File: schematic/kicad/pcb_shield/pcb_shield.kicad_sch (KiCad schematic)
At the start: 1 part, among them U1 NUCLEO64-F411RE

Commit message: pcb schematic
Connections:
- net BL_MOTOR_A: now also U1.44 (PC5); no longer U1.62 (PB1)
- net BL_MOTOR_B: now also U1.1 (PC10); no longer U1.60 (PB2)
- net BR_MOTOR_A: now also U1.2 (PC11); no longer U1.54 (PB12)
- net BR_MOTOR_B: now also U1.3 (PC12); no longer U1.44 (PC5)
- net FL_MOTOR_A: now also U1.38 (PC0); no longer U1.72 (PC4)
- net FL_MOTOR_B: now also U1.36 (PC1); no longer U1.68 (PB13)
- net FR_ENCODER_A: now also U1.51 (PA6); no longer U1.65 (PB4)
- net FR_ENCODER_B: now also U1.53 (PA7); no longer U1.57 (PC7)
- net FR_MOTOR_A: now also U1.35 (PC2); no longer U1.66 (PB14)
- net FR_MOTOR_B: now also U1.37 (PC3); no longer U1.64 (PB15)
- net GND: now also U1.19 (GND), U1.20 (GND), U1.22 (GND), U1.47 (GND), U1.58 (GND), U1.77 (GND), U1.78 (GND), U1.79 (GND), U1.80 (GND)
- net +12V: no longer names the net of U1.24 (VIN)
- net +5V: no longer names the net of U1.18 (+5V)
- net STM32_RX6: no longer names the net of U1.50 (PA12)
- net STM32_TX6 renamed TX6
- new net RX6: U1.57 (PC7)

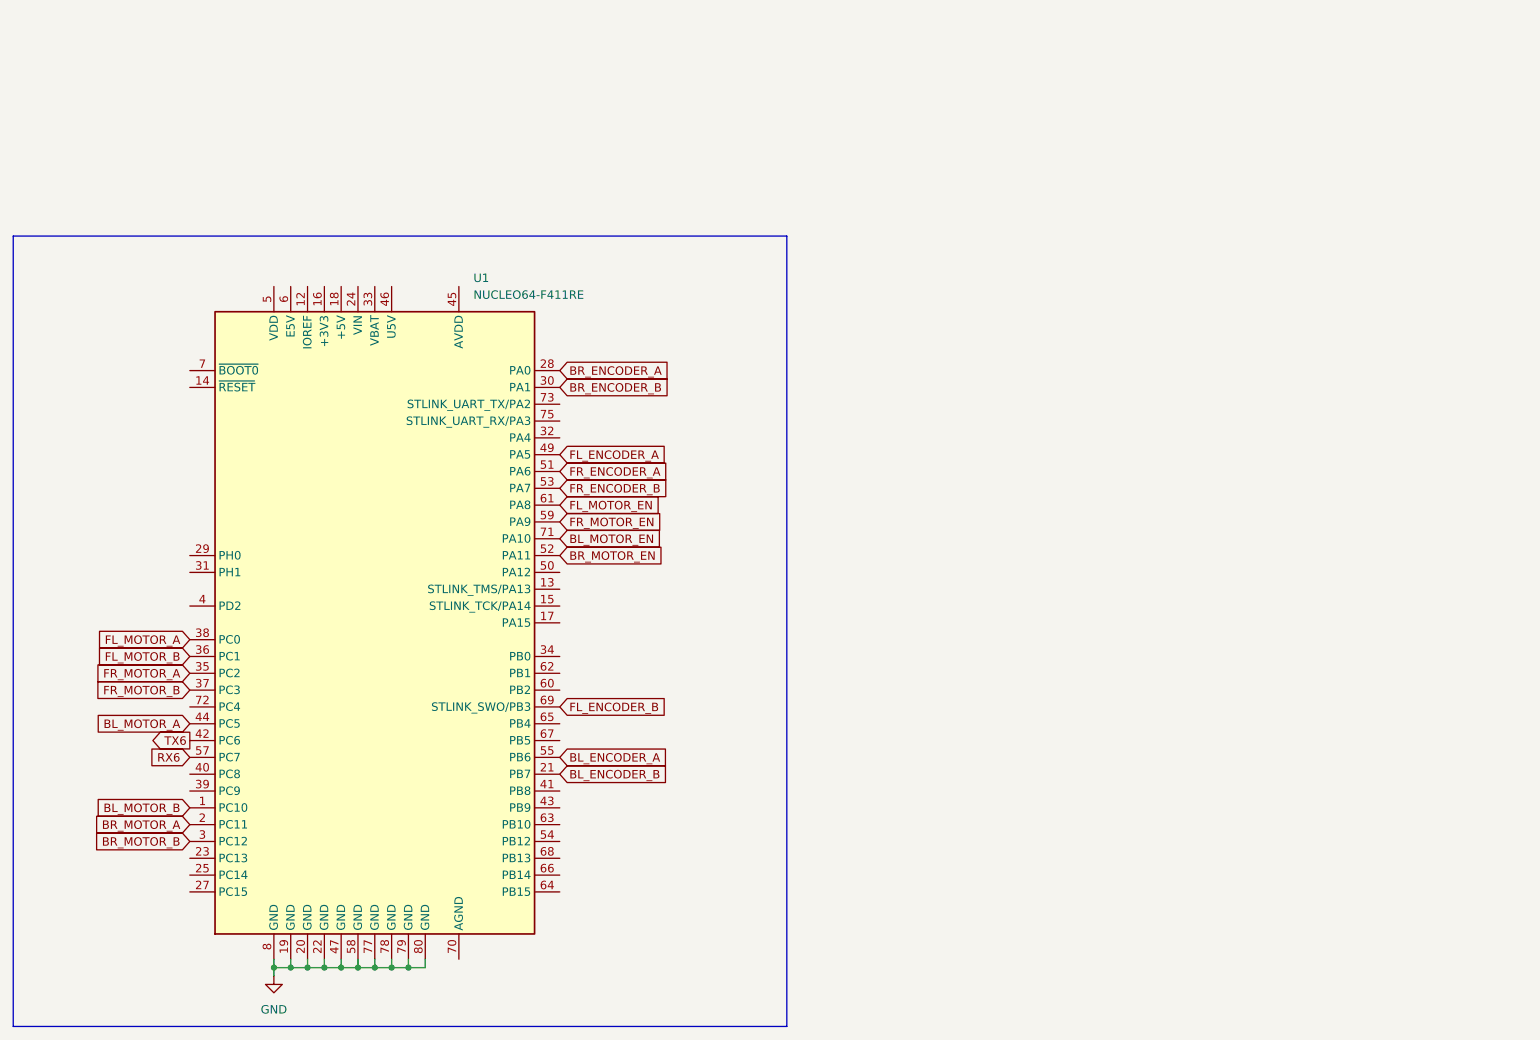
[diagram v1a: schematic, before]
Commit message: progress with code and pcb shield
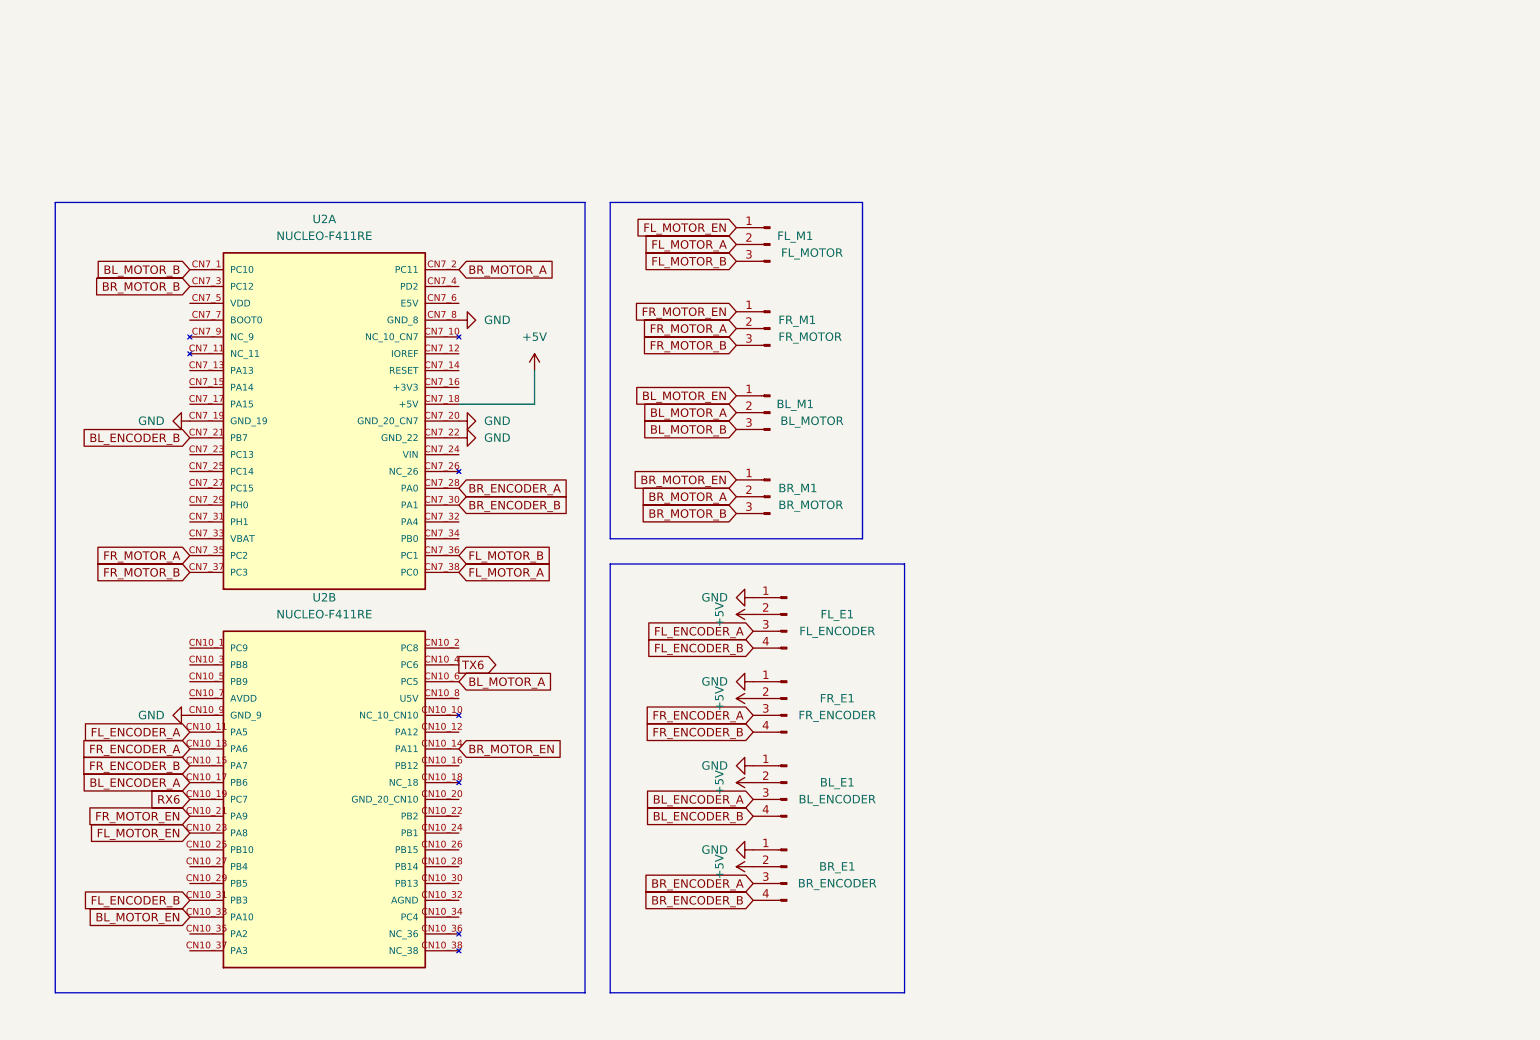
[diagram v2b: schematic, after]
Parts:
- removed U1: NUCLEO64-F411RE, Module:ST_Morpho_Connector_144_STLink, symbol MCU_Module:NUCLEO64-F411RE
- added BL_E1: BL_ENCODER, Connector_PinHeader_2.54mm:PinHeader_1x04_P2.54mm_Vertical, symbol Connector:Conn_01x04_Pin
- added BL_M1: BL_MOTOR, Connector_PinHeader_2.54mm:PinHeader_1x03_P2.54mm_Vertical, symbol Connector:Conn_01x03_Pin
- added BR_E1: BR_ENCODER, Connector_PinHeader_2.54mm:PinHeader_1x04_P2.54mm_Vertical, symbol Connector:Conn_01x04_Pin
- added BR_M1: BR_MOTOR, Connector_PinHeader_2.54mm:PinHeader_1x03_P2.54mm_Vertical, symbol Connector:Conn_01x03_Pin
- added FL_E1: FL_ENCODER, Connector_PinHeader_2.54mm:PinHeader_1x04_P2.54mm_Vertical, symbol Connector:Conn_01x04_Pin
- added FL_M1: FL_MOTOR, Connector_PinHeader_2.54mm:PinHeader_1x03_P2.54mm_Vertical, symbol Connector:Conn_01x03_Pin
- added FR_E1: FR_ENCODER, Connector_PinHeader_2.54mm:PinHeader_1x04_P2.54mm_Vertical, symbol Connector:Conn_01x04_Pin
- added FR_M1: FR_MOTOR, Connector_PinHeader_2.54mm:PinHeader_1x03_P2.54mm_Vertical, symbol Connector:Conn_01x03_Pin
- added U2: NUCLEO-F411RE, NUCLEO-F411RE:BOARD_NUCLEO-F411RE_custom, symbol NUCLEO-F411RE:NUCLEO-F411RE
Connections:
- net BL_ENCODER_A: now also BL_E1.3 (Pin_3), U2.CN10_17 (PB6)
- net BL_ENCODER_B: now also BL_E1.4 (Pin_4), U2.CN7_21 (PB7)
- net BL_MOTOR_A: now also BL_M1.2 (Pin_2), U2.CN10_6 (PC5)
- net BL_MOTOR_B: now also BL_M1.3 (Pin_3), U2.CN7_1 (PC10)
- net BL_MOTOR_EN: now also BL_M1.1 (Pin_1), U2.CN10_33 (PA10)
- net BR_ENCODER_A: now also BR_E1.3 (Pin_3), U2.CN7_28 (PA0)
- net BR_ENCODER_B: now also BR_E1.4 (Pin_4), U2.CN7_30 (PA1)
- net BR_MOTOR_A: now also BR_M1.2 (Pin_2), U2.CN7_2 (PC11)
- net BR_MOTOR_B: now also BR_M1.3 (Pin_3), U2.CN7_3 (PC12)
- net BR_MOTOR_EN: now also BR_M1.1 (Pin_1), U2.CN10_14 (PA11)
- net FL_ENCODER_A: now also FL_E1.3 (Pin_3), U2.CN10_11 (PA5)
- net FL_ENCODER_B: now also FL_E1.4 (Pin_4), U2.CN10_31 (PB3)
- net FL_MOTOR_A: now also FL_M1.2 (Pin_2), U2.CN7_38 (PC0)
- net FL_MOTOR_B: now also FL_M1.3 (Pin_3), U2.CN7_36 (PC1)
- net FL_MOTOR_EN: now also FL_M1.1 (Pin_1), U2.CN10_23 (PA8)
- net FR_ENCODER_A: now also FR_E1.3 (Pin_3), U2.CN10_13 (PA6)
- net FR_ENCODER_B: now also FR_E1.4 (Pin_4), U2.CN10_15 (PA7)
- net FR_MOTOR_A: now also FR_M1.2 (Pin_2), U2.CN7_35 (PC2)
- net FR_MOTOR_B: now also FR_M1.3 (Pin_3), U2.CN7_37 (PC3)
- net FR_MOTOR_EN: now also FR_M1.1 (Pin_1), U2.CN10_21 (PA9)
- net GND: now also BL_E1.1 (Pin_1), BR_E1.1 (Pin_1), FL_E1.1 (Pin_1), FR_E1.1 (Pin_1), U2.CN10_9 (GND_9), U2.CN7_19 (GND_19), U2.CN7_20 (GND_20_CN7), U2.CN7_22 (GND_22), U2.CN7_8 (GND_8)
- net RX6: now also U2.CN10_19 (PC7)
- net TX6: now also U2.CN10_4 (PC6)
- new net +5V: BL_E1.2 (Pin_2), BR_E1.2 (Pin_2), FL_E1.2 (Pin_2), FR_E1.2 (Pin_2), U2.CN7_18 (+5V)
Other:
- title: (none) -> Rover mecanum nucleo f411re v2 pcb shield

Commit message: change shield template1
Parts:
- removed U2: NUCLEO-F411RE, NUCLEO-F411RE:BOARD_NUCLEO-F411RE_custom, symbol NUCLEO-F411RE:NUCLEO-F411RE
- added H1, H2, H3: MountingHole, MountingHole:MountingHole_3.2mm_M3, symbol Mechanical:MountingHole
- added J1: CN7, Connector_PinSocket_2.54mm:PinSocket_2x19_P2.54mm_Vertical, symbol Connector_Generic:Conn_02x19_Odd_Even
- added J2: CN10, Connector_PinSocket_2.54mm:PinSocket_2x19_P2.54mm_Vertical, symbol Connector_Generic:Conn_02x19_Odd_Even
- added PWR: POWER, symbol Connector:Conn_01x03_Pin
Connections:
- net +5V: now also J1.18 (Pin_18), PWR.2 (Pin_2)
- net BL_ENCODER_A: now also J2.17 (Pin_17)
- net BL_ENCODER_B: now also J1.21 (Pin_21)
- net BL_MOTOR_A: now also J2.6 (Pin_6)
- net BL_MOTOR_B: now also J1.1 (Pin_1)
- net BL_MOTOR_EN: now also J2.33 (Pin_33)
- net BR_ENCODER_A: now also J1.28 (Pin_28)
- net BR_ENCODER_B: now also J1.30 (Pin_30)
- net BR_MOTOR_A: now also J1.2 (Pin_2)
- net BR_MOTOR_B: now also J1.3 (Pin_3)
- net BR_MOTOR_EN: now also J2.14 (Pin_14)
- net FL_ENCODER_A: now also J2.11 (Pin_11)
- net FL_ENCODER_B: now also J2.31 (Pin_31)
- net FL_MOTOR_A: now also J1.38 (Pin_38)
- net FL_MOTOR_B: now also J1.36 (Pin_36)
- net FL_MOTOR_EN: now also J2.23 (Pin_23)
- net FR_ENCODER_A: now also J2.13 (Pin_13)
- net FR_ENCODER_B: now also J2.15 (Pin_15)
- net FR_MOTOR_A: now also J1.35 (Pin_35)
- net FR_MOTOR_B: now also J1.37 (Pin_37)
- net FR_MOTOR_EN: now also J2.21 (Pin_21)
- net GND: now also J1.19 (Pin_19), J1.20 (Pin_20), J1.22 (Pin_22), J1.8 (Pin_8), J2.20 (Pin_20), J2.9 (Pin_9), PWR.1 (Pin_1)
- new net +12V: PWR.3 (Pin_3)
- new net +3V3: J1.16 (Pin_16)
- new net +BATT: J1.33 (Pin_33)
- new net 5V_USB_CHGR: J2.8 (Pin_8)
- new net BOOT0: J1.7 (Pin_7)
- new net E5V: J1.6 (Pin_6)
- new net GNDA: J2.32 (Pin_32)
- new net IOREF: J1.12 (Pin_12)
- new net PA12: J2.12 (Pin_12)
- new net PA13: J1.13 (Pin_13)
- new net PA14: J1.15 (Pin_15)
- new net PA15: J1.17 (Pin_17)
- new net PA2: J2.35 (Pin_35)
- new net PA3: J2.37 (Pin_37)
- new net PA4: J1.32 (Pin_32)
- new net PB0: J1.34 (Pin_34)
- new net PB1: J2.24 (Pin_24)
- new net PB10: J2.25 (Pin_25)
- new net PB12: J2.16 (Pin_16)
- new net PB13: J2.30 (Pin_30)
- new net PB14: J2.28 (Pin_28)
- new net PB15: J2.26 (Pin_26)
- new net PB2: J2.22 (Pin_22)
- new net PB4: J2.27 (Pin_27)
- new net PB5: J2.29 (Pin_29)
- new net PB8: J2.3 (Pin_3)
- new net PB9: J2.5 (Pin_5)
- new net PC13: J1.23 (Pin_23)
- new net PC14: J1.25 (Pin_25)
- new net PC15: J1.27 (Pin_27)
- new net PC4: J2.34 (Pin_34)
- new net PC6: J2.4 (Pin_4)
- new net PC7: J2.19 (Pin_19)
- new net PC8: J2.2 (Pin_2)
- new net PC9: J2.1 (Pin_1)
- new net PD2: J1.4 (Pin_4)
- new net PH0: J1.29 (Pin_29)
- new net PH1: J1.31 (Pin_31)
- new net VDD: J1.5 (Pin_5)
- new net VDDA: J2.7 (Pin_7)
- new net VIN: J1.24 (Pin_24)
- new net ~{RST}: J1.14 (Pin_14)
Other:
- note added: "Mechanical"
- title: Rover mecanum nucleo f411re v2 pcb shield -> (none)

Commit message: first working versio
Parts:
- PWR1: renamed from PWR; footprint (none) -> Connector_PinHeader_2.54mm:PinHeader_1x03_P2.54mm_Vertical
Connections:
- net VIN is gone; now on net +12V: J1.24 (Pin_24)
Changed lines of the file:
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@@
+    (stroke (width 0) (type default))
+  )
+  (wire (pts (xy 162.56 40.005) (xy 165.735 40.005))
     (stroke (width 0) (type default))
   )
@@
   )
   (wire (pts (xy 87.63 50.165) (xy 76.835 50.165))
+    (stroke (width 0) (type default))
+  )
+  (wire (pts (xy 165.735 40.005) (xy 165.735 36.83))
     (stroke (width 0) (type default))
   )
@@
   (label "VIN" (at 102.235 73.025 0) (fields_autoplaced)
     (effects (font (size 1.27 1.27)) (justify left bottom))
+  )
+  (label "VIN" (at 162.56 40.005 180) (fields_autoplaced)
+    (effects (font (size 1.27 1.27)) (justify right bottom))
   )
   (label "PA0" (at 100.33 78.105 0) (fields_autoplaced)
@@
         (path "/da5a1e6a-2605-436b-a30c-1027586d5c0a"
           (reference "FR_M1") (unit 1)
+        )
+      )
+    )
+  )
+  (symbol (lib_id "power:+12V") (at 165.735 36.83 0) (unit 1)
+    (in_bom yes) (on_board yes) (dnp no)
+    (property "Reference" "#PWR04" (at 165.735 40.64 0)
+      (effects (font (size 1.27 1.27)) hide)
+    )
+    (property "Value" "+12V" (at 165.735 33.02 90)
+      (effects (font (size 1.27 1.27)) (justify left))
+    )
+    (property "Footprint" "" (at 165.735 36.83 0)
+      (effects (font (size 1.27 1.27)) hide)
+    )
+    (property "Datasheet" "" (at 165.735 36.83 0)
+      (effects (font (size 1.27 1.27)) hide)
+    )
+    (pin "1")
+    (instances
+      (project "pcb_shield"
+        (path "/da5a1e6a-2605-436b-a30c-1027586d5c0a"
+          (reference "#PWR04") (unit 1)
         )
       )
@@
   (symbol (lib_id "Connector:Conn_01x03_Pin") (at 145.415 40.64 0) (mirror y) (unit 1)
     (in_bom yes) (on_board yes) (dnp no)
-    (property "Reference" "PWR" (at 149.86 39.37 0)
+    (property "Reference" "PWR1" (at 149.86 39.37 0)
       (effects (font (size 1.27 1.27)))
     )
@@
       (effects (font (size 1.27 1.27)))
     )
-    (property "Footprint" "" (at 145.415 40.64 0)
+    (property "Footprint" "Connector_PinHeader_2.54mm:PinHeader_1x03_P2.54mm_Vertical" (at 145.415 40.64 0)
       (effects (font (size 1.27 1.27)) hide)
     )
@@
       (project "pcb_shield"
         (path "/da5a1e6a-2605-436b-a30c-1027586d5c0a"
-          (reference "PWR") (unit 1)
-        )
-      )
+          (reference "PWR1") (unit 1)
+        )
+      )

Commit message: first actual working version
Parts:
- added CTRL_UART1: CTRL_UART, Connector_PinHeader_2.54mm:PinHeader_1x04_P2.54mm_Vertical, symbol Connector:Conn_01x04_Pin
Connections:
- net +5V: now also CTRL_UART1.2 (Pin_2)
- net GND: now also CTRL_UART1.1 (Pin_1)
- net PC6 renamed TX6
- net TX6: now also CTRL_UART1.3 (Pin_3)
- net PC7 renamed RX6
- net RX6: now also CTRL_UART1.4 (Pin_4)

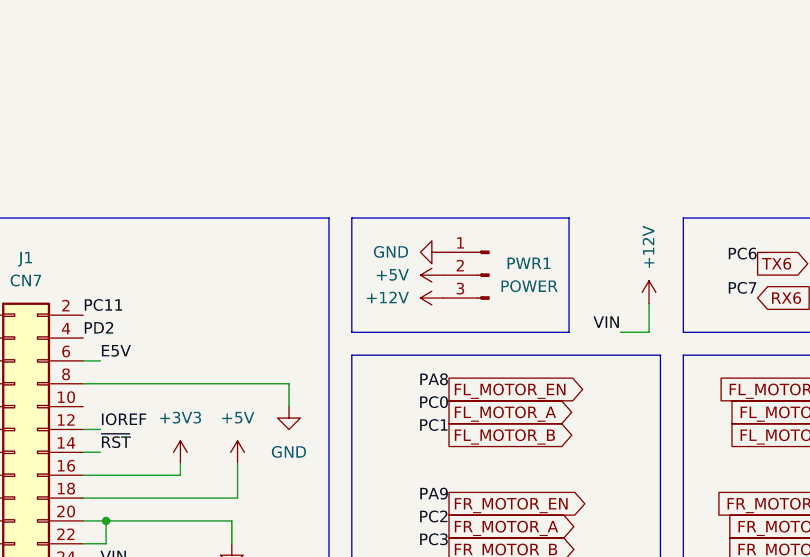
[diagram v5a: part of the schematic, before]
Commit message: fix power input connector
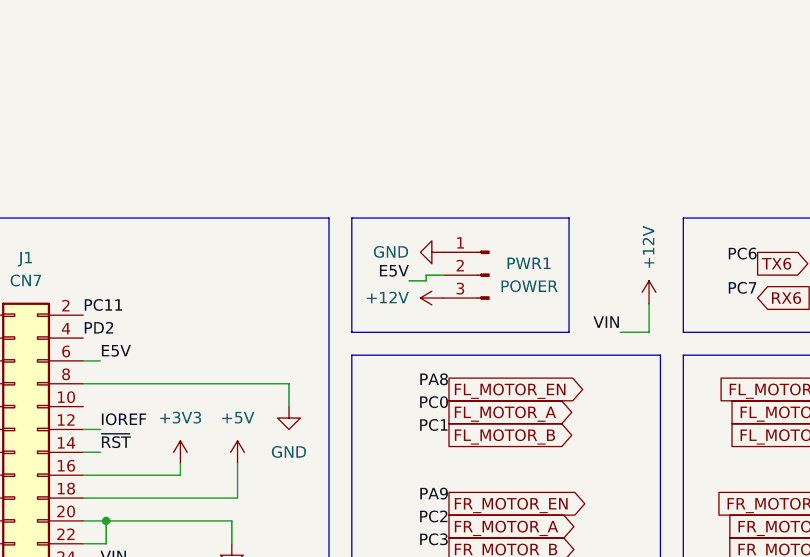
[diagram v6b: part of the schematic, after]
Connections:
- net +5V: no longer PWR1.2 (Pin_2)
- net E5V: now also PWR1.2 (Pin_2)
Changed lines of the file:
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@@
+    (stroke (width 0) (type default))
+  )
+  (wire (pts (xy 138.43 41.275) (xy 138.43 40.64))
     (stroke (width 0) (type default))
   )
@@
     (stroke (width 0) (type default))
   )
+  (wire (pts (xy 136.525 41.275) (xy 138.43 41.275))
+    (stroke (width 0) (type default))
+  )
   (wire (pts (xy 100.33 60.325) (xy 102.235 60.325))
+    (stroke (width 0) (type default))
+  )
+  (wire (pts (xy 138.43 40.64) (xy 140.335 40.64))
     (stroke (width 0) (type default))
   )
@@
   )
   (label "PC3" (at 140.97 71.12 180) (fields_autoplaced)
+    (effects (font (size 1.27 1.27)) (justify right bottom))
+  )
+  (label "E5V" (at 136.525 41.275 180) (fields_autoplaced)
     (effects (font (size 1.27 1.27)) (justify right bottom))
   )
@@
         )
       )
-    )
-  )
-  (symbol (lib_name "+5V_1") (lib_id "power:+5V") (at 140.335 40.64 90) (unit 1)
-    (in_bom yes) (on_board yes) (dnp no) (fields_autoplaced)
-    (property "Reference" "#PWR02" (at 144.145 40.64 0)
-      (effects (font (size 1.27 1.27)) hide)
-    )
-    (property "Value" "+5V" (at 136.525 40.64 90)
-      (effects (font (size 1.27 1.27)) (justify left))
-    )
-    (property "Footprint" "" (at 140.335 40.64 0)
-      (effects (font (size 1.27 1.27)) hide)
-    )
-    (property "Datasheet" "" (at 140.335 40.64 0)
-      (effects (font (size 1.27 1.27)) hide)
-    )
-    (pin "1")
-    (instances
-      (project "pcb_shield"
-        (path "/da5a1e6a-2605-436b-a30c-1027586d5c0a"
-          (reference "#PWR02") (unit 1)
-        )
-      )
